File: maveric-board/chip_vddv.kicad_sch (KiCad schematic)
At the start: 9 parts, among them U3 Socket

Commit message: swap some extended parts out for basic ones
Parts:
- C27, C28, C29, C30, C31, C32, C33, C34: value 10uF -> 10u; JLCPCB Part # C95839 -> C19702; Mfr Part # CL10A106KQ8NNNC -> CL10A106KP8NNNC
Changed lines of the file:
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@@
 			)
 		)
-		(property "Value" "10uF"
+		(property "Value" "10u"
 			(at 91.44 91.4399 0)
 			(effects
@@
 			)
 		)
-		(property "JLCPCB Part #" "C95839"
+		(property "JLCPCB Part #" "C19702"
 			(at 87.63 90.17 0)
 			(effects
@@
 			)
 		)
-		(property "Mfr Part #" "CL10A106KQ8NNNC"
+		(property "Mfr Part #" "CL10A106KP8NNNC"
 			(at 100.584 93.98 0)
 			(effects
@@
 			)
 		)
-		(property "Value" "10uF"
+		(property "Value" "10u"
 			(at 19.05 91.4399 0)
 			(effects
@@
 			)
 		)
-		(property "JLCPCB Part #" "C95839"
+		(property "JLCPCB Part #" "C19702"
 			(at 15.24 90.17 0)
 			(effects
@@
 			)
 		)
-		(property "Mfr Part #" "CL10A106KQ8NNNC"
+		(property "Mfr Part #" "CL10A106KP8NNNC"
 			(at 28.194 93.98 0)
 			(effects
@@
 			)
 		)
-		(property "Value" "10uF"
+		(property "Value" "10u"
 			(at 21.59 31.7499 0)
 			(effects
@@
 			)
 		)
-		(property "JLCPCB Part #" "C95839"
+		(property "JLCPCB Part #" "C19702"
 			(at 17.78 30.48 0)
 			(effects
@@
 			)
 		)
-		(property "Mfr Part #" "CL10A106KQ8NNNC"
+		(property "Mfr Part #" "CL10A106KP8NNNC"
 			(at 30.734 34.29 0)
 			(effects
@@
 			)
 		)
-		(property "Value" "10uF"
+		(property "Value" "10u"
 			(at 189.23 31.7499 0)
 			(effects
@@
 			)
 		)
-		(property "JLCPCB Part #" "C95839"
+		(property "JLCPCB Part #" "C19702"
 			(at 185.42 30.48 0)
 			(effects
@@
 			)
 		)
-		(property "Mfr Part #" "CL10A106KQ8NNNC"
+		(property "Mfr Part #" "CL10A106KP8NNNC"
 			(at 198.374 34.29 0)
 			(effects
@@
 			)
 		)
-		(property "Value" "10uF"
+		(property "Value" "10u"
 			(at 93.98 31.7499 0)
 			(effects
@@
 			)
 		)
-		(property "JLCPCB Part #" "C95839"
+		(property "JLCPCB Part #" "C19702"
 			(at 90.17 30.48 0)
 			(effects
@@
 			)
 		)
-		(property "Mfr Part #" "CL10A106KQ8NNNC"
+		(property "Mfr Part #" "CL10A106KP8NNNC"
 			(at 103.124 34.29 0)
 			(effects
@@
 			)
 		)
-		(property "Value" "10uF"
+		(property "Value" "10u"
 			(at 116.84 91.4399 0)
 			(effects
@@
 			)
 		)
-		(property "JLCPCB Part #" "C95839"
+		(property "JLCPCB Part #" "C19702"
 			(at 113.03 90.17 0)
 			(effects
@@
 			)
 		)
-		(property "Mfr Part #" "CL10A106KQ8NNNC"
+		(property "Mfr Part #" "CL10A106KP8NNNC"
 			(at 125.984 93.98 0)
 			(effects
@@
 			)
 		)
-		(property "Value" "10uF"
+		(property "Value" "10u"
 			(at 118.11 31.7499 0)
 			(effects
@@
 			)
 		)
-		(property "JLCPCB Part #" "C95839"
+		(property "JLCPCB Part #" "C19702"
 			(at 114.3 30.48 0)
 			(effects
@@
 			)
 		)
-		(property "Mfr Part #" "CL10A106KQ8NNNC"
+		(property "Mfr Part #" "CL10A106KP8NNNC"
 			(at 127.254 34.29 0)
 			(effects
@@
 			)
 		)
-		(property "Value" "10uF"
+		(property "Value" "10u"
 			(at 187.96 91.4399 0)
 			(effects
@@
 			)
 		)
-		(property "JLCPCB Part #" "C95839"
+		(property "JLCPCB Part #" "C19702"
 			(at 184.15 90.17 0)
 			(effects
@@
 			)
 		)
-		(property "Mfr Part #" "CL10A106KQ8NNNC"
+		(property "Mfr Part #" "CL10A106KP8NNNC"
 			(at 197.104 93.98 0)
 			(effects

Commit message: resync all symbols to schematic, reannotate schematic
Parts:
- renumbered C27 to C28, C28 to C29, C29 to C30, C30 to C31, C31 to C32, C32 to C33, C33 to C34, C34 to C35
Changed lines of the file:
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@@
 		(dnp no)
 		(fields_autoplaced yes)
-		(property "Reference" "#PWR069"
+		(property "Reference" "#PWR074"
 			(at 85.09 22.86 0)
 			(effects
@@
 			(project "maveric-board"
 				(path "/ae861d46-65fb-4872-932f-ad48addb0154/e298f94f-7e65-4ace-92f5-b6c14efcef75"
-					(reference "#PWR069")
+					(reference "#PWR074")
 					(unit 1)
 				)
@@
 		(dnp no)
 		(fields_autoplaced yes)
-		(property "Reference" "#PWR079"
+		(property "Reference" "#PWR084"
 			(at 185.42 43.18 0)
 			(effects
@@
 			(project "maveric-board"
 				(path "/ae861d46-65fb-4872-932f-ad48addb0154/e298f94f-7e65-4ace-92f5-b6c14efcef75"
-					(reference "#PWR079")
+					(reference "#PWR084")
 					(unit 1)
 				)
@@
 		(dnp no)
 		(fields_autoplaced yes)
-		(property "Reference" "#PWR070"
+		(property "Reference" "#PWR075"
 			(at 87.63 102.87 0)
 			(effects
@@
 			(project "maveric-board"
 				(path "/ae861d46-65fb-4872-932f-ad48addb0154/e298f94f-7e65-4ace-92f5-b6c14efcef75"
-					(reference "#PWR070")
+					(reference "#PWR075")
 					(unit 1)
 				)
@@
 		(dnp no)
 		(fields_autoplaced yes)
-		(property "Reference" "#PWR077"
+		(property "Reference" "#PWR082"
 			(at 180.34 22.86 0)
 			(effects
@@
 			(project "maveric-board"
 				(path "/ae861d46-65fb-4872-932f-ad48addb0154/e298f94f-7e65-4ace-92f5-b6c14efcef75"
-					(reference "#PWR077")
+					(reference "#PWR082")
 					(unit 1)
 				)
@@
 		(dnp no)
 		(fields_autoplaced yes)
-		(property "Reference" "#PWR066"
+		(property "Reference" "#PWR071"
 			(at 39.37 82.55 0)
 			(effects
@@
 			(project "maveric-board"
 				(path "/ae861d46-65fb-4872-932f-ad48addb0154/e298f94f-7e65-4ace-92f5-b6c14efcef75"
-					(reference "#PWR066")
+					(reference "#PWR071")
 					(unit 1)
 				)
@@
 		(on_board yes)
 		(dnp no)
-		(property "Reference" "C29"
+		(property "Reference" "C30"
 			(at 91.44 88.8999 0)
 			(effects
@@
 			)
 		)
-		(property "Datasheet" ""
+		(property "Datasheet" "~"
 			(at 87.63 90.17 0)
 			(effects
@@
 			(project "maveric-board"
 				(path "/ae861d46-65fb-4872-932f-ad48addb0154/e298f94f-7e65-4ace-92f5-b6c14efcef75"
-					(reference "C29")
+					(reference "C30")
 					(unit 1)
 				)
@@
 		(on_board yes)
 		(dnp no)
-		(property "Reference" "C27"
+		(property "Reference" "C28"
 			(at 19.05 88.8999 0)
 			(effects
@@
 			)
 		)
-		(property "Datasheet" ""
+		(property "Datasheet" "~"
 			(at 15.24 90.17 0)
 			(effects
@@
 			(project "maveric-board"
 				(path "/ae861d46-65fb-4872-932f-ad48addb0154/e298f94f-7e65-4ace-92f5-b6c14efcef75"
-					(reference "C27")
+					(reference "C28")
 					(unit 1)
 				)
@@
 		(dnp no)
 		(fields_autoplaced yes)
-		(property "Reference" "#PWR071"
+		(property "Reference" "#PWR076"
 			(at 90.17 43.18 0)
 			(effects
@@
 			(project "maveric-board"
 				(path "/ae861d46-65fb-4872-932f-ad48addb0154/e298f94f-7e65-4ace-92f5-b6c14efcef75"
-					(reference "#PWR071")
+					(reference "#PWR076")
 					(unit 1)
 				)
@@
 		(dnp no)
 		(fields_autoplaced yes)
-		(property "Reference" "#PWR074"
+		(property "Reference" "#PWR079"
 			(at 135.89 82.55 0)
 			(effects
@@
 			(project "maveric-board"
 				(path "/ae861d46-65fb-4872-932f-ad48addb0154/e298f94f-7e65-4ace-92f5-b6c14efcef75"
-					(reference "#PWR074")
+					(reference "#PWR079")
 					(unit 1)
 				)
@@
 		(dnp no)
 		(fields_autoplaced yes)
-		(property "Reference" "#PWR068"
+		(property "Reference" "#PWR073"
 			(at 82.55 82.55 0)
 			(effects
@@
 			(project "maveric-board"
 				(path "/ae861d46-65fb-4872-932f-ad48addb0154/e298f94f-7e65-4ace-92f5-b6c14efcef75"
-					(reference "#PWR068")
+					(reference "#PWR073")
 					(unit 1)
 				)
@@
 		(on_board yes)
 		(dnp no)
-		(property "Reference" "C28"
+		(property "Reference" "C29"
 			(at 21.59 29.2099 0)
 			(effects
@@
 			)
 		)
-		(property "Datasheet" ""
+		(property "Datasheet" "~"
 			(at 17.78 30.48 0)
 			(effects
@@
 			(project "maveric-board"
 				(path "/ae861d46-65fb-4872-932f-ad48addb0154/e298f94f-7e65-4ace-92f5-b6c14efcef75"
-					(reference "C28")
+					(reference "C29")
 					(unit 1)
 				)
@@
 		(on_board yes)
 		(dnp no)
-		(property "Reference" "C34"
+		(property "Reference" "C35"
 			(at 189.23 29.2099 0)
 			(effects
@@
 			)
 		)
-		(property "Datasheet" ""
+		(property "Datasheet" "~"
 			(at 185.42 30.48 0)
 			(effects
@@
 			(project "maveric-board"
 				(path "/ae861d46-65fb-4872-932f-ad48addb0154/e298f94f-7e65-4ace-92f5-b6c14efcef75"
-					(reference "C34")
+					(reference "C35")
 					(unit 1)
 				)
@@
 		(dnp no)
 		(fields_autoplaced yes)
-		(property "Reference" "#PWR076"
+		(property "Reference" "#PWR081"
 			(at 179.07 82.55 0)
 			(effects
@@
 			(project "maveric-board"
 				(path "/ae861d46-65fb-4872-932f-ad48addb0154/e298f94f-7e65-4ace-92f5-b6c14efcef75"
-					(reference "#PWR076")
+					(reference "#PWR081")
 					(unit 1)
 				)
@@
 		(on_board yes)
 		(dnp no)
-		(property "Reference" "C30"
+		(property "Reference" "C31"
 			(at 93.98 29.2099 0)
 			(effects
@@
 			)
 		)
-		(property "Datasheet" ""
+		(property "Datasheet" "~"
 			(at 90.17 30.48 0)
 			(effects
@@
 			(project "maveric-board"
 				(path "/ae861d46-65fb-4872-932f-ad48addb0154/e298f94f-7e65-4ace-92f5-b6c14efcef75"
-					(reference "C30")
+					(reference "C31")
 					(unit 1)
 				)
@@
 		(dnp no)
 		(fields_autoplaced yes)
-		(property "Reference" "#PWR075"
+		(property "Reference" "#PWR080"
 			(at 137.16 22.86 0)
 			(effects
@@
 			(project "maveric-board"
 				(path "/ae861d46-65fb-4872-932f-ad48addb0154/e298f94f-7e65-4ace-92f5-b6c14efcef75"
-					(reference "#PWR075")
+					(reference "#PWR080")
 					(unit 1)
 				)
@@
 		(dnp no)
 		(fields_autoplaced yes)
-		(property "Reference" "#PWR064"
+		(property "Reference" "#PWR069"
 			(at 15.24 102.87 0)
 			(effects
@@
 			(project "maveric-board"
 				(path "/ae861d46-65fb-4872-932f-ad48addb0154/e298f94f-7e65-4ace-92f5-b6c14efcef75"
-					(reference "#PWR064")
+					(reference "#PWR069")
 					(unit 1)
 				)
@@
 		(on_board yes)
 		(dnp no)
-		(property "Reference" "C31"
+		(property "Reference" "C32"
 			(at 116.84 88.8999 0)
 			(effects
@@
 			)
 		)
-		(property "Datasheet" ""
+		(property "Datasheet" "~"
 			(at 113.03 90.17 0)
 			(effects
@@
 			(project "maveric-board"
 				(path "/ae861d46-65fb-4872-932f-ad48addb0154/e298f94f-7e65-4ace-92f5-b6c14efcef75"
-					(reference "C31")
+					(reference "C32")
 					(unit 1)
 				)
@@
 		(dnp no)
 		(fields_autoplaced yes)
-		(property "Reference" "#PWR067"
+		(property "Reference" "#PWR072"
 			(at 41.91 22.86 0)
 			(effects
@@
 			(project ""
 				(path "/ae861d46-65fb-4872-932f-ad48addb0154/e298f94f-7e65-4ace-92f5-b6c14efcef75"
-					(reference "#PWR067")
+					(reference "#PWR072")
 					(unit 1)
 				)
@@
 		(on_board yes)
 		(dnp no)
-		(property "Reference" "C32"
+		(property "Reference" "C33"
 			(at 118.11 29.2099 0)
 			(effects
@@
 			)
 		)
-		(property "Datasheet" ""
+		(property "Datasheet" "~"
 			(at 114.3 30.48 0)
 			(effects
@@
 			(project "maveric-board"
 				(path "/ae861d46-65fb-4872-932f-ad48addb0154/e298f94f-7e65-4ace-92f5-b6c14efcef75"
-					(reference "C32")
+					(reference "C33")
 					(unit 1)
 				)
@@
 		(dnp no)
 		(fields_autoplaced yes)
-		(property "Reference" "#PWR078"
+		(property "Reference" "#PWR083"
 			(at 184.15 102.87 0)
 			(effects
@@
 			(project "maveric-board"
 				(path "/ae861d46-65fb-4872-932f-ad48addb0154/e298f94f-7e65-4ace-92f5-b6c14efcef75"
-					(reference "#PWR078")
+					(reference "#PWR083")
 					(unit 1)
 				)
@@
 		(dnp no)
 		(fields_autoplaced yes)
-		(property "Reference" "#PWR072"
+		(property "Reference" "#PWR077"
 			(at 113.03 102.87 0)
 			(effects
@@
 			(project "maveric-board"
 				(path "/ae861d46-65fb-4872-932f-ad48addb0154/e298f94f-7e65-4ace-92f5-b6c14efcef75"
-					(reference "#PWR072")
+					(reference "#PWR077")
 					(unit 1)
 				)
@@
 		(dnp no)
 		(fields_autoplaced yes)
-		(property "Reference" "#PWR073"
+		(property "Reference" "#PWR078"
 			(at 114.3 43.18 0)
 			(effects
@@
 			(project "maveric-board"
 				(path "/ae861d46-65fb-4872-932f-ad48addb0154/e298f94f-7e65-4ace-92f5-b6c14efcef75"
-					(reference "#PWR073")
+					(reference "#PWR078")
 					(unit 1)
 				)
@@
 		(on_board yes)
 		(dnp no)
-		(property "Reference" "C33"
+		(property "Reference" "C34"
 			(at 187.96 88.8999 0)
 			(effects
@@
 			)
 		)
-		(property "Datasheet" ""
+		(property "Datasheet" "~"
 			(at 184.15 90.17 0)
 			(effects
@@
 			(project "maveric-board"
 				(path "/ae861d46-65fb-4872-932f-ad48addb0154/e298f94f-7e65-4ace-92f5-b6c14efcef75"
-					(reference "C33")
+					(reference "C34")
 					(unit 1)
 				)
@@
 		(dnp no)
 		(fields_autoplaced yes)
-		(property "Reference" "#PWR065"
+		(property "Reference" "#PWR070"
 			(at 17.78 43.18 0)
 			(effects
@@
 			(project "maveric-board"
 				(path "/ae861d46-65fb-4872-932f-ad48addb0154/e298f94f-7e65-4ace-92f5-b6c14efcef75"
-					(reference "#PWR065")
+					(reference "#PWR070")
 					(unit 1)
 				)

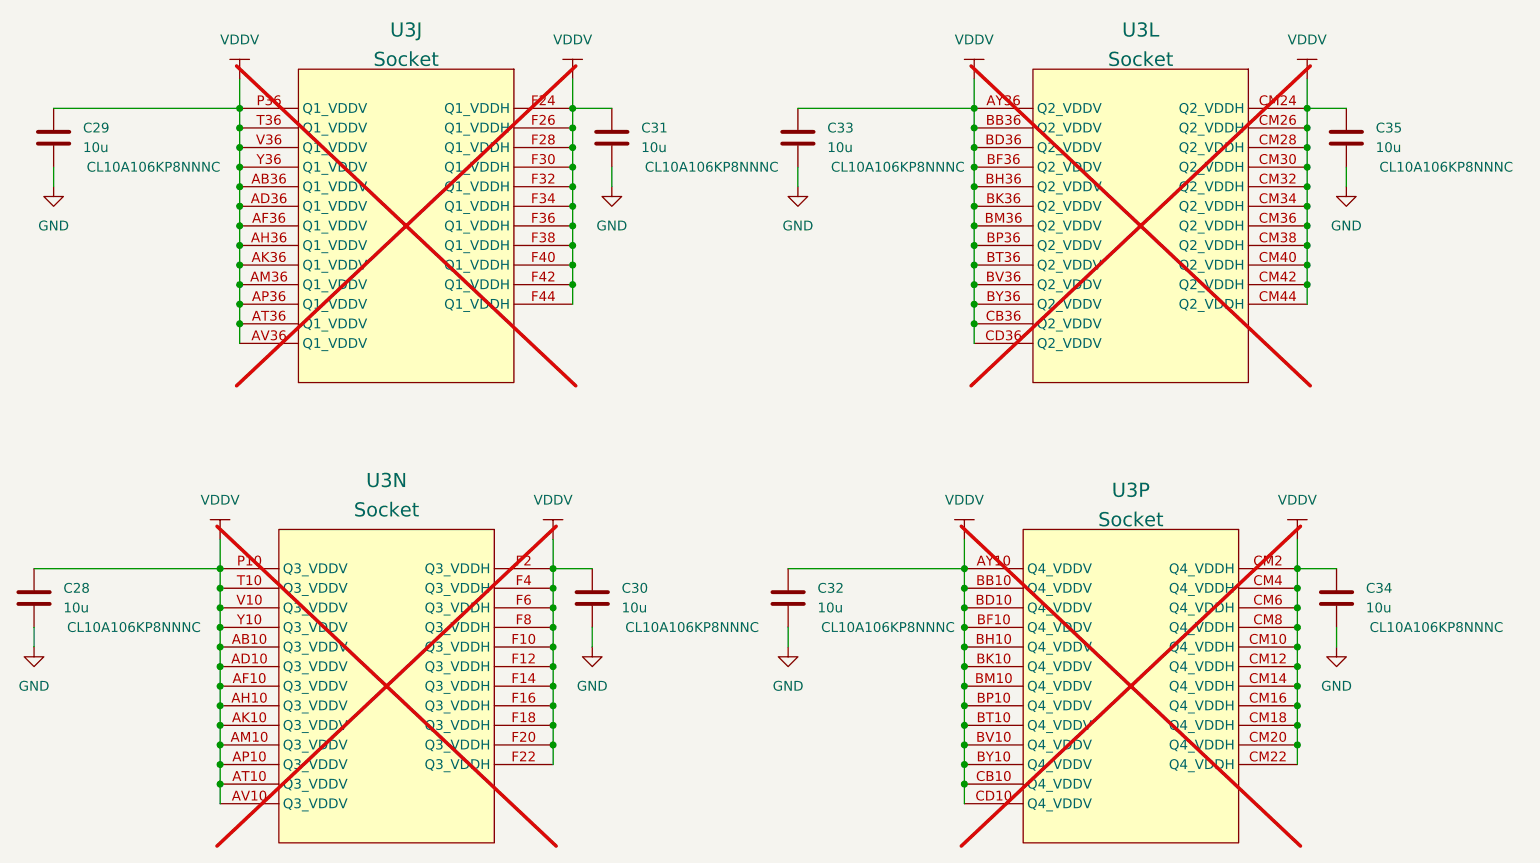
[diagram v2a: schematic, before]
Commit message: fixup schematic + redo banana jack footprints to match jlc render
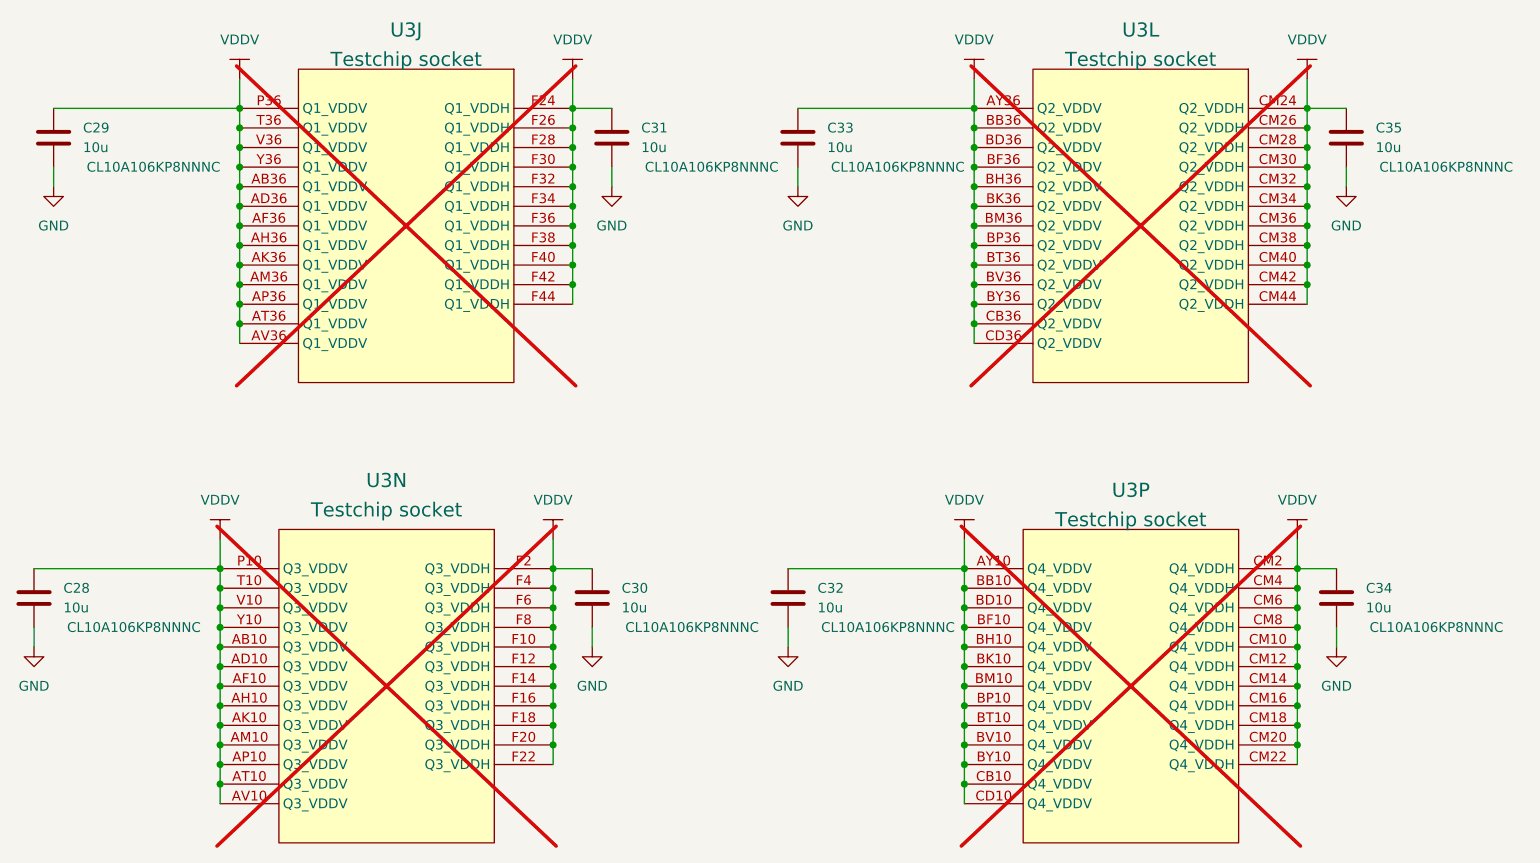
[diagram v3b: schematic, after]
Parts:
- U3: value Socket -> Testchip socket
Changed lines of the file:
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@@
 			)
 		)
-		(property "Value" "Socket"
+		(property "Value" "Testchip socket"
 			(at 158.75 20.32 0)
 			(effects
@@
 			)
 		)
-		(property "Value" "Socket"
+		(property "Value" "Testchip socket"
 			(at 60.96 78.74 0)
 			(effects
@@
 			)
 		)
-		(property "Value" "Socket"
+		(property "Value" "Testchip socket"
 			(at 63.5 20.32 0)
 			(effects
@@
 			)
 		)
-		(property "Value" "Socket"
+		(property "Value" "Testchip socket"
 			(at 157.48 80.01 0)
 			(effects
